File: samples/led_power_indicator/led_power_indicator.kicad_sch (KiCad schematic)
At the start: 7 parts, among them J1 USB-C, U1 TLV75518

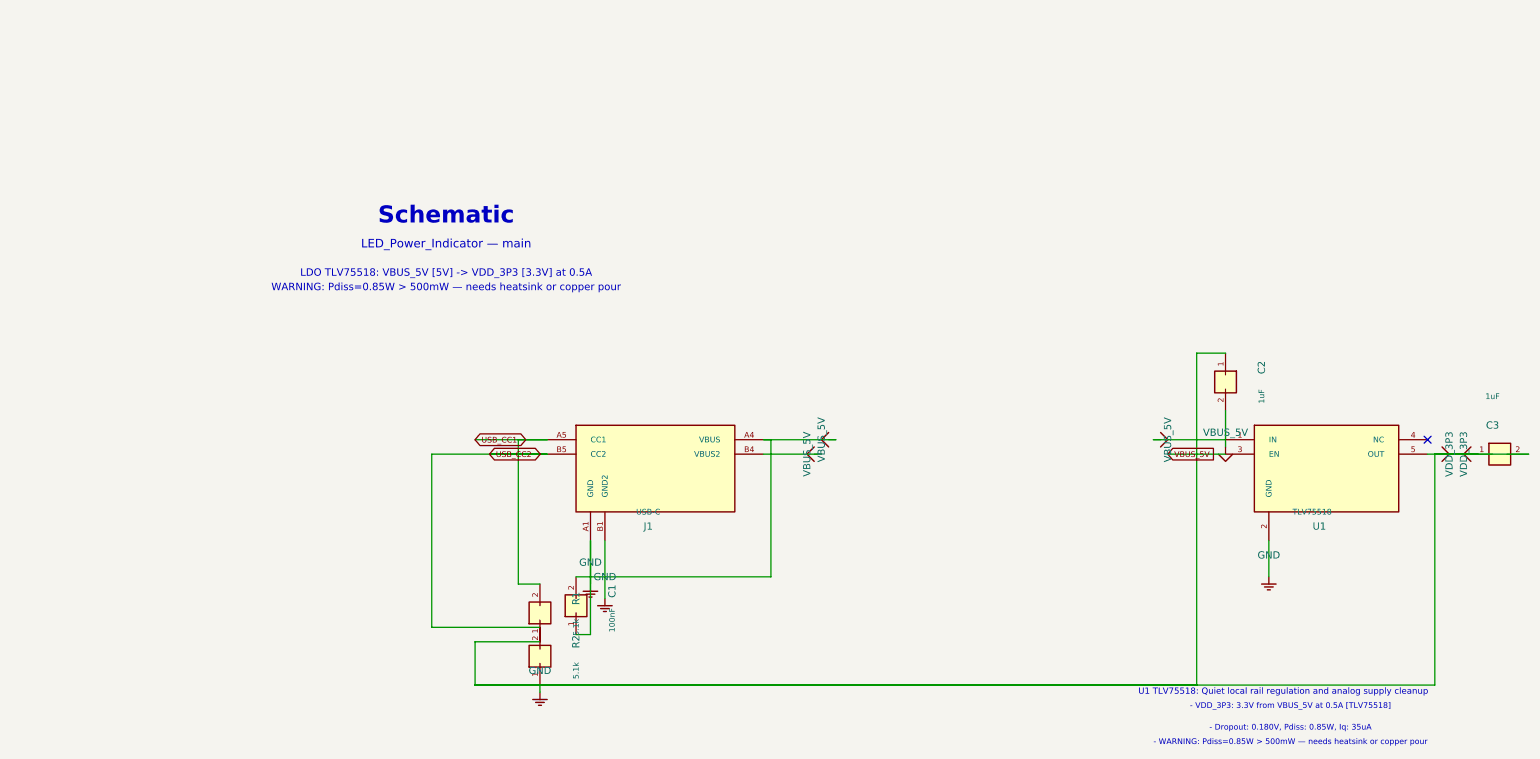
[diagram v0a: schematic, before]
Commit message: chore: regenerate 8 sample designs against v0.27.0 engine
All 8 samples pass full validation (0 ERC errors):
- led_power_indicator, iot_sensor_node, usb_regulated_supply,
  usb_uart_bridge, oled_display_module, battery_iot_sensor,
  motor_controller, fpga_power_carrier

New artifacts per sample: .kicad_sch, _test_points.csv, _pinout.csv,
canonical_spec.yaml, design_ir.json, validation_report.json; MCU samples
also emit sdkconfig.defaults / .ioc stubs.

Also adds samples/*/svg/ to .gitignore — schematic SVG exports are
regenerable and too large to track.

zigbee_humidistat deferred: non-deterministic schematic output across
two generation runs (text annotation ordering vs sheet_instances).
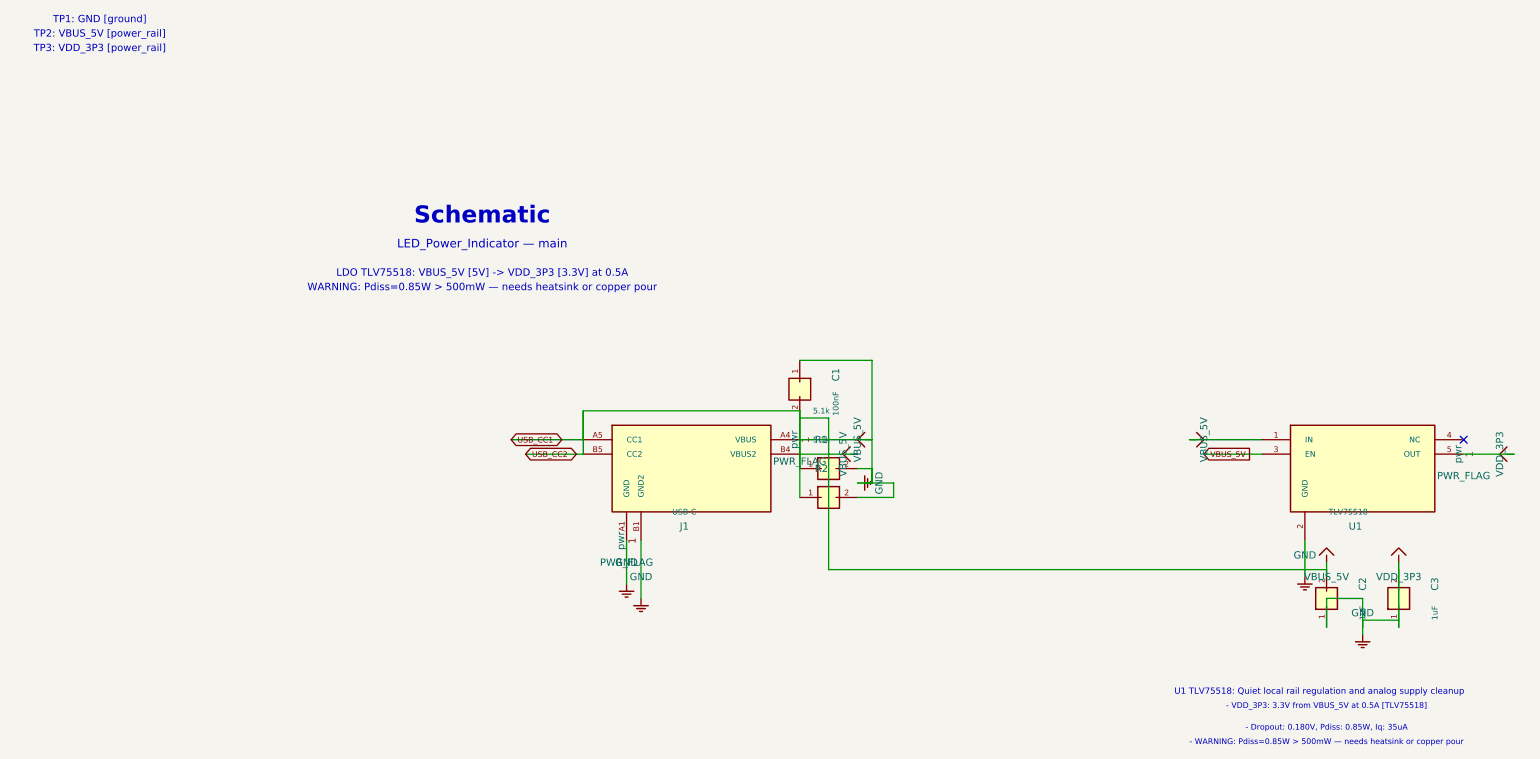
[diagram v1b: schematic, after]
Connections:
- net GND: now also R1.2, R2.2; no longer R1.1, R2.1
- net USB_CC1: now also J1.B5 (CC2), R1.1, R2.1; no longer R1.2
- removed net USB_CC2: J1.B5 (CC2), R2.2
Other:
- note added: "TP1: GND [ground]"
- note added: "TP2: VBUS_5V [power_rail]"
- note added: "TP3: VDD_3P3 [power_rail]"
- moved on the sheet: C1, J1, U1
